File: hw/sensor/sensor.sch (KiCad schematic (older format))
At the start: 30 parts, among them J1 TC2030-CTX, U1 NRF52811-QFAA, U2 SHT3x-DIS, Y1 32.768kHz, Y2 32MHz

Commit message: Finished ostur sensor and released to oshpark
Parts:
- AE1: DKPN (none) -> 535-14095-1-ND; MPN (none) -> AMCA31-2R450G-S1F-T3
- BT1: DKPN (none) -> BK-912-ND; MPN (none) -> BK-912
- D1, D2: DKPN (none) -> 1516-1216-1-ND; MPN (none) -> QBLP595-IG
- R1, R2: DKPN (none) -> 311-10KJRCT-ND; MPN (none) -> RC0402JR-0710KL
- R5: DKPN (none) -> 1276-3480-1-ND; MPN (none) -> RC1005J000CS
- U2: DKPN (none) -> 1649-1082-1-ND; MPN (none) -> SHT30-DIS-P2.5KS
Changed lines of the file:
@@
 F 2 "alvarop:AMCA31-2R450G-S1F-T3" H 12900 5950 50  0001 C CNN
 F 3 "~" H 12900 5950 50  0001 C CNN
+F 4 "535-14095-1-ND" H 12900 5950 50  0001 C CNN "DKPN"
+F 5 "AMCA31-2R450G-S1F-T3" H 12900 5950 50  0001 C CNN "MPN"
 	1    12900 5950
 	1    0    0    -1
@@
 F 2 "Resistor_SMD:R_0402_1005Metric" H 12500 6250 50  0001 C CNN
 F 3 "~" H 12500 6250 50  0001 C CNN
+F 4 "1276-3480-1-ND" H 12500 6250 50  0001 C CNN "DKPN"
+F 5 "RC1005J000CS" H 12500 6250 50  0001 C CNN "MPN"
 	1    12500 6250
 	0    1    1    0
@@
 F 2 "alvarop:BK-912" V 4400 2410 50  0001 C CNN
 F 3 "~" V 4400 2410 50  0001 C CNN
+F 4 "BK-912-ND" H 4400 2350 50  0001 C CNN "DKPN"
+F 5 "BK-912" H 4400 2350 50  0001 C CNN "MPN"
 	1    4400 2350
 	1    0    0    -1
@@
 F 2 "Resistor_SMD:R_0402_1005Metric" H 5050 6200 50  0001 C CNN
 F 3 "~" H 5050 6200 50  0001 C CNN
+F 4 "311-10KJRCT-ND" H 5050 6200 50  0001 C CNN "DKPN"
+F 5 "RC0402JR-0710KL" H 5050 6200 50  0001 C CNN "MPN"
 	1    5050 6200
 	-1   0    0    1
@@
 F 2 "Resistor_SMD:R_0402_1005Metric" H 4800 6200 50  0001 C CNN
 F 3 "~" H 4800 6200 50  0001 C CNN
+F 4 "311-10KJRCT-ND" H 4800 6200 50  0001 C CNN "DKPN"
+F 5 "RC0402JR-0710KL" H 4800 6200 50  0001 C CNN "MPN"
 	1    4800 6200
 	-1   0    0    1
@@
 F 2 "LED_SMD:LED_0402_1005Metric" H 4800 6600 50  0001 C CNN
 F 3 "~" H 4800 6600 50  0001 C CNN
+F 4 "1516-1216-1-ND" H 4800 6600 50  0001 C CNN "DKPN"
+F 5 "QBLP595-IG" H 4800 6600 50  0001 C CNN "MPN"
 	1    4800 6600
 	0    -1   -1   0
@@
 F 2 "LED_SMD:LED_0402_1005Metric" H 5050 6600 50  0001 C CNN
 F 3 "~" H 5050 6600 50  0001 C CNN
+F 4 "1516-1216-1-ND" H 5050 6600 50  0001 C CNN "DKPN"
+F 5 "QBLP595-IG" H 5050 6600 50  0001 C CNN "MPN"
 	1    5050 6600
 	0    -1   -1   0
@@
 F 2 "alvarop:SHT3x" H 8950 9050 60  0001 C CNN
 F 3 "" H 8950 9050 60  0000 C CNN
+F 4 "1649-1082-1-ND" H 9200 9050 50  0001 C CNN "DKPN"
+F 5 "SHT30-DIS-P2.5KS" H 9200 9050 50  0001 C CNN "MPN"
 	1    9200 9050
 	1    0    0    -1

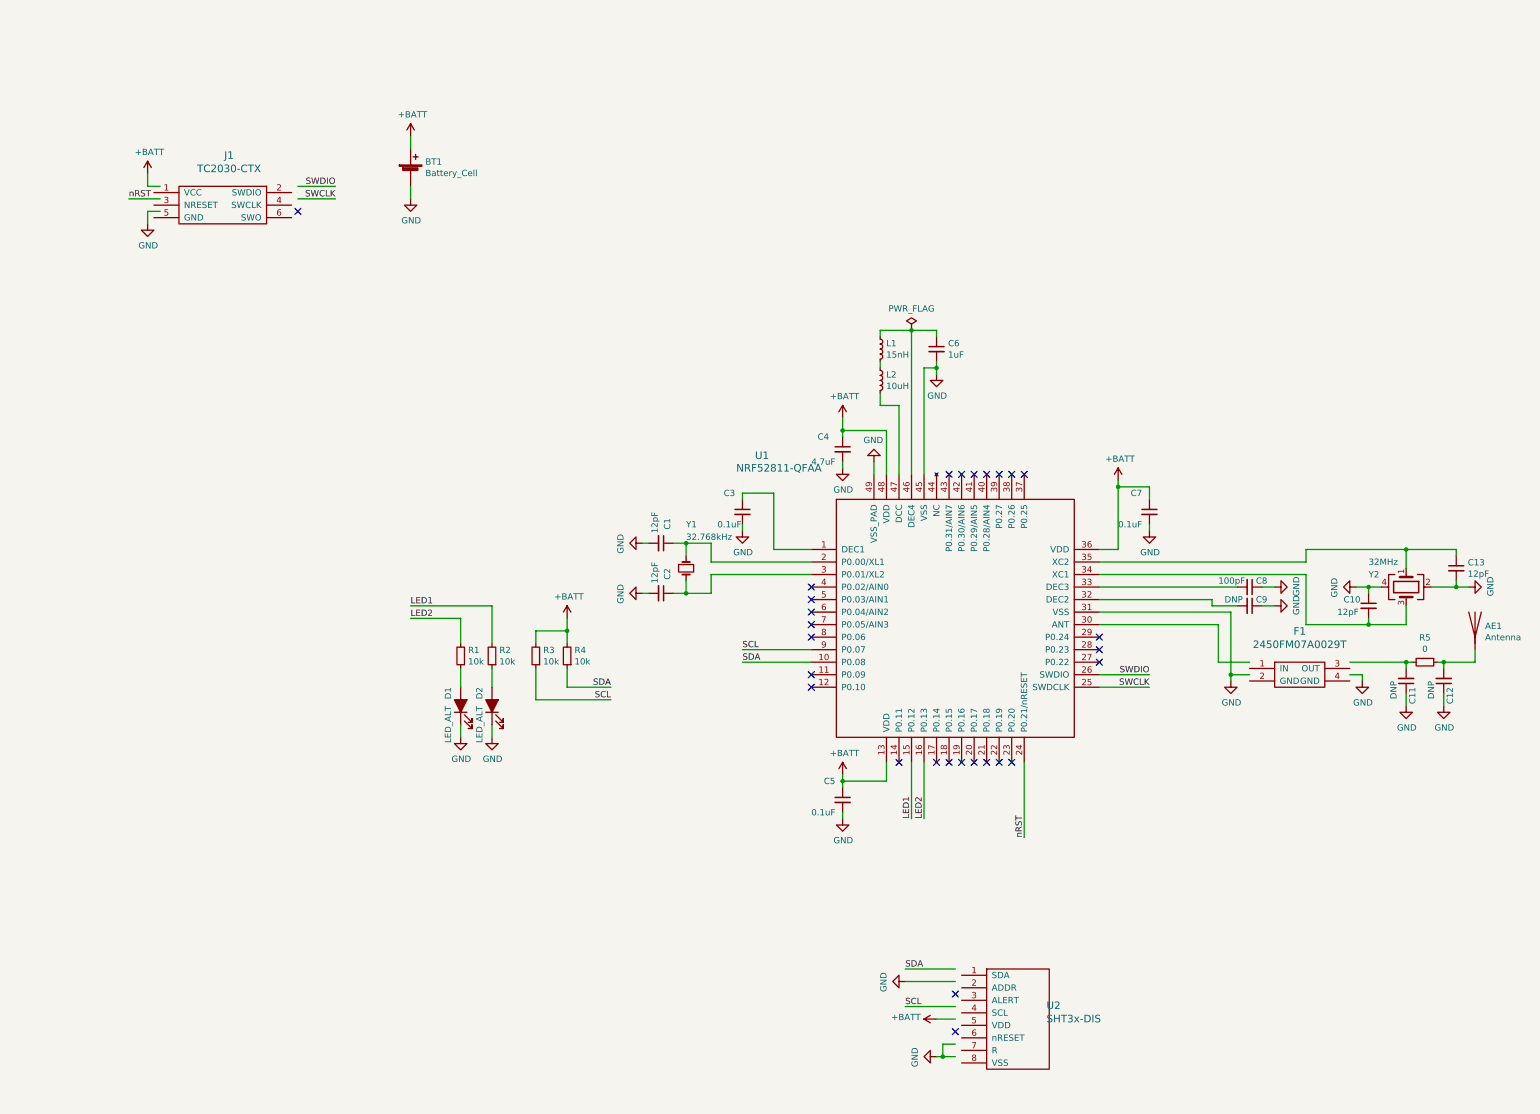
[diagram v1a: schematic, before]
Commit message: Released Ostur Sensor v1.1 to JLCPCB
Changes:
* Changed to 4 layer board for better RF performance
* Changed RF trace to match 50Ohms on JLCPCB's JLC7628 stackup
* Added decoupling capacitor for SHT3x
* Changed I2C pull-ups to 0402's
* Fixed silkscreen issues
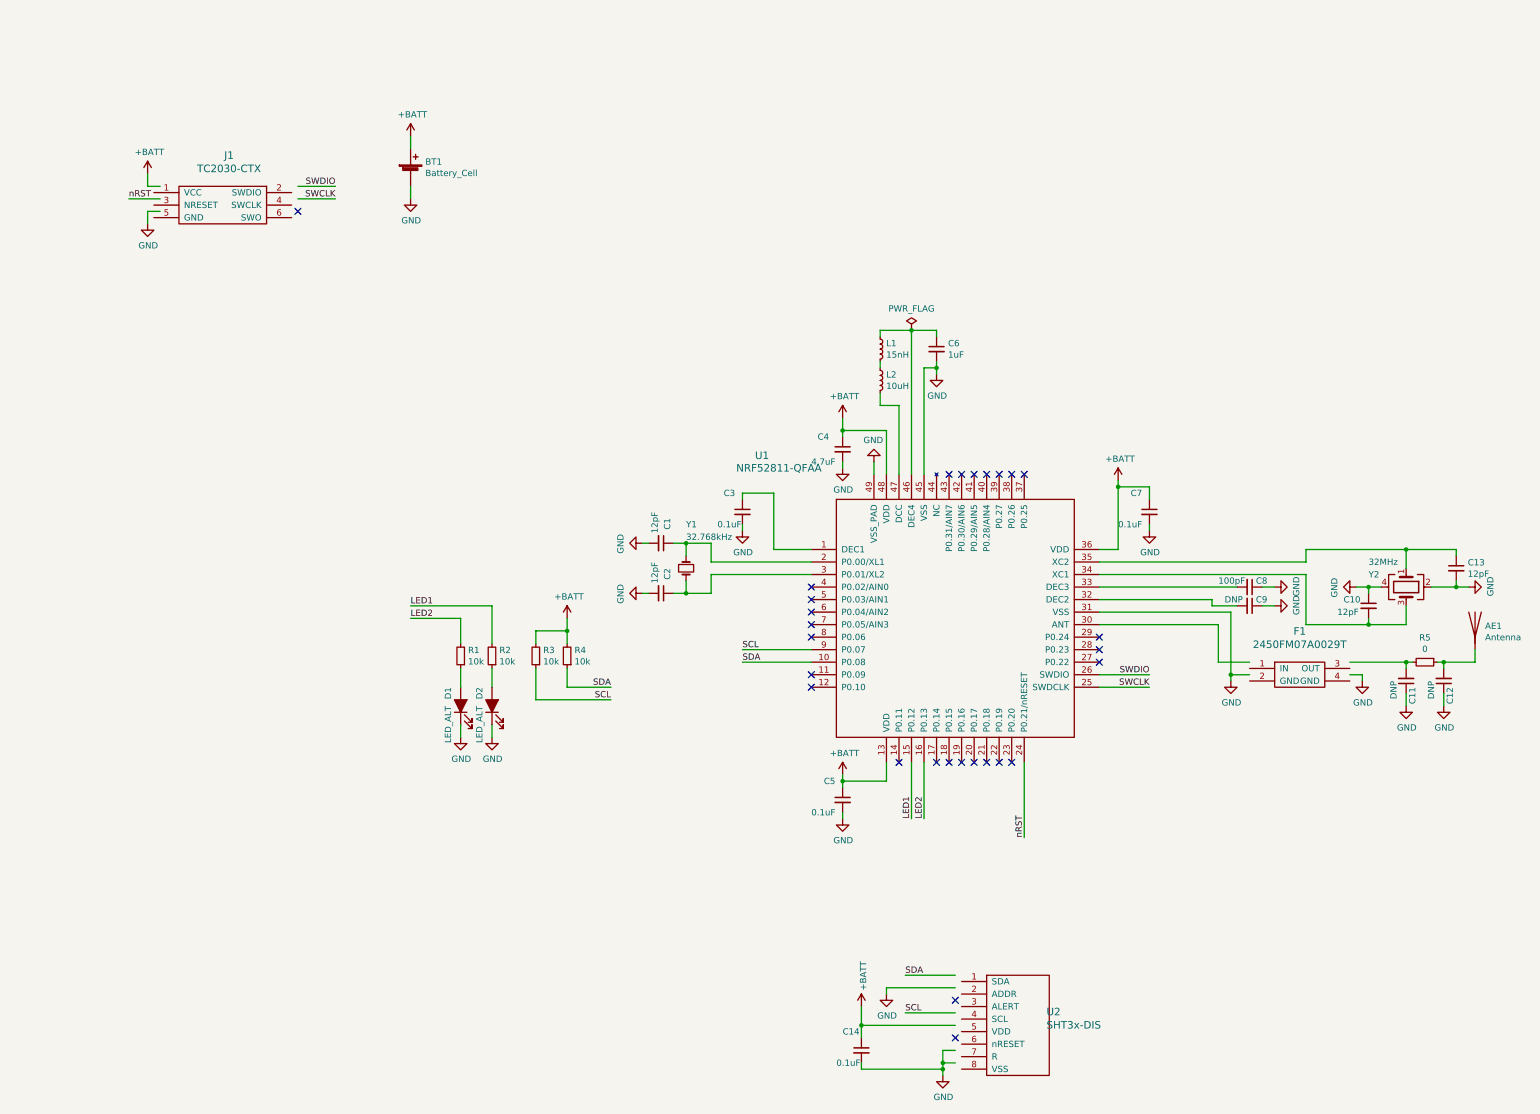
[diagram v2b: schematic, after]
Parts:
- added C14: 0.1uF, Capacitor_SMD:C_0402_1005Metric, symbol Device:C_Small
- R3, R4: footprint Resistor_SMD:R_0603_1608Metric -> Resistor_SMD:R_0402_1005Metric; DKPN (none) -> 311-10KJRCT-ND; MPN (none) -> RC0402JR-0710KL
- U1: footprint Package_DFN_QFN:QFN-48-1EP_6x6mm_P0.4mm_EP4.6x4.6mm -> alvarop:NRF52811-QFN48
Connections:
- wire segments 129 -> 135
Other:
- moved on the sheet: U2
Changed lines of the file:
@@
 EESchema Schematic File Version 4
 LIBS:sensor-cache
-EELAYER 29 0
+EELAYER 30 0
 EELAYER END
 $Descr A3 16535 11693
@@
 Sheet 1 1
 Title "Ostur Sensor"
-Date "2019-06-29"
-Rev "1.0"
+Date "2019-10-10"
+Rev "1.1"
 Comp "@alvaroprieto"
 Comment1 ""
@@
 	2400 2450 2300 2450
 Wire Wire Line
-	2300 2450 2300 2350
-Wire Wire Line
 	2400 2550 2150 2550
 Wire Wire Line
 	2400 2650 2300 2650
-Wire Wire Line
-	2300 2650 2300 2750
 $Comp
 L power:GND #PWR02
@@
 F 0 "U1" H 7150 7200 60  0000 L CNN
 F 1 "NRF52811-QFAA" H 7000 7100 60  0000 L CNN
-F 2 "Package_DFN_QFN:QFN-48-1EP_6x6mm_P0.4mm_EP4.6x4.6mm" H 7600 6450 50  0001 C CNN
+F 2 "alvarop:NRF52811-QFN48" H 7600 6450 50  0001 C CNN
 F 3 "" H 7600 6450 50  0001 C CNN
 F 4 "‎1490-1075-1-ND‎" H 8750 5900 50  0001 C CNN "DKPN"
@@
 L power:+BATT #PWR018
 U 1 1 5D1FA7C1
-P 8600 9100
-F 0 "#PWR018" H 8600 8950 50  0001 C CNN
-F 1 "+BATT" V 8615 9227 50  0000 L CNN
-F 2 "" H 8600 9100 50  0001 C CNN
-F 3 "" H 8600 9100 50  0001 C CNN
-	1    8600 9100
-	0    -1   -1   0
+P 8000 9000
+F 0 "#PWR018" H 8000 8850 50  0001 C CNN
+F 1 "+BATT" V 8015 9127 50  0000 L CNN
+F 2 "" H 8000 9000 50  0001 C CNN
+F 3 "" H 8000 9000 50  0001 C CNN
+	1    8000 9000
+	1    0    0    -1
 $EndComp
 $Comp
 L power:GND #PWR019
 U 1 1 5D1FD0BD
-P 8600 9400
-F 0 "#PWR019" H 8600 9150 50  0001 C CNN
-F 1 "GND" H 8605 9227 50  0000 C CNN
-F 2 "" H 8600 9400 50  0001 C CNN
-F 3 "" H 8600 9400 50  0001 C CNN
-	1    8600 9400
-	0    1    1    0
-$EndComp
-Wire Wire Line
-	8750 9400 8650 9400
-Wire Wire Line
-	8750 9100 8600 9100
-Wire Wire Line
-	8750 8700 8350 8700
-Wire Wire Line
-	8750 8800 8350 8800
-Wire Wire Line
-	8750 9000 8350 9000
-Wire Wire Line
-	8650 9300 8650 9400
-Wire Wire Line
-	8650 9300 8750 9300
-Connection ~ 8650 9400
-Wire Wire Line
-	8650 9400 8600 9400
+P 8650 9550
+F 0 "#PWR019" H 8650 9300 50  0001 C CNN
+F 1 "GND" H 8655 9377 50  0000 C CNN
+F 2 "" H 8650 9550 50  0001 C CNN
+F 3 "" H 8650 9550 50  0001 C CNN
+	1    8650 9550
+	1    0    0    -1
+$EndComp
+Wire Wire Line
+	8750 9450 8650 9450
+Wire Wire Line
+	8750 8750 8350 8750
+Wire Wire Line
+	8750 9050 8350 9050
+Wire Wire Line
+	8650 9350 8650 9450
+Wire Wire Line
+	8650 9350 8750 9350
+Connection ~ 8650 9450
+Wire Wire Line
+	8650 9450 8650 9500
 $Comp
 L power:GND #PWR016
 U 1 1 5D22F6D9
-P 8350 8800
-F 0 "#PWR016" H 8350 8550 50  0001 C CNN
-F 1 "GND" H 8355 8627 50  0000 C CNN
-F 2 "" H 8350 8800 50  0001 C CNN
-F 3 "" H 8350 8800 50  0001 C CNN
-	1    8350 8800
-	0    1    1    0
-$EndComp
-NoConn ~ 8750 8900
-Text Label 8350 8700 0    50   ~ 0
+P 8200 8900
+F 0 "#PWR016" H 8200 8650 50  0001 C CNN
+F 1 "GND" H 8205 8727 50  0000 C CNN
+F 2 "" H 8200 8900 50  0001 C CNN
+F 3 "" H 8200 8900 50  0001 C CNN
+	1    8200 8900
+	1    0    0    -1
+$EndComp
+NoConn ~ 8750 8950
+Text Label 8350 8750 0    50   ~ 0
 SDA
-Text Label 8350 9000 0    50   ~ 0
+Text Label 8350 9050 0    50   ~ 0
 SCL
 NoConn ~ 9900 6250
@@
 F 0 "R4" H 5591 6154 50  0000 R CNN
 F 1 "10k" H 5591 6245 50  0000 R CNN
-F 2 "Resistor_SMD:R_0603_1608Metric" H 5650 6200 50  0001 C CNN
+F 2 "Resistor_SMD:R_0402_1005Metric" H 5650 6200 50  0001 C CNN
 F 3 "~" H 5650 6200 50  0001 C CNN
+F 4 "311-10KJRCT-ND" H 5650 6200 50  0001 C CNN "DKPN"
+F 5 "RC0402JR-0710KL" H 5650 6200 50  0001 C CNN "MPN"
 	1    5650 6200
 	-1   0    0    1
@@
 F 0 "R3" H 5341 6154 50  0000 R CNN
 F 1 "10k" H 5341 6245 50  0000 R CNN
-F 2 "Resistor_SMD:R_0603_1608Metric" H 5400 6200 50  0001 C CNN
+F 2 "Resistor_SMD:R_0402_1005Metric" H 5400 6200 50  0001 C CNN
 F 3 "~" H 5400 6200 50  0001 C CNN
+F 4 "311-10KJRCT-ND" H 5400 6200 50  0001 C CNN "DKPN"
+F 5 "RC0402JR-0710KL" H 5400 6200 50  0001 C CNN "MPN"
 	1    5400 6200
 	-1   0    0    1
@@
 L alvarop:SHT3x-DIS U2
 U 1 1 5D1DABB6
-P 9200 9050
-F 0 "U2" H 9478 9108 60  0000 L CNN
-F 1 "SHT3x-DIS" H 9478 9002 60  0000 L CNN
-F 2 "alvarop:SHT3x" H 8950 9050 60  0001 C CNN
-F 3 "" H 8950 9050 60  0000 C CNN
-F 4 "1649-1082-1-ND" H 9200 9050 50  0001 C CNN "DKPN"
-F 5 "SHT30-DIS-P2.5KS" H 9200 9050 50  0001 C CNN "MPN"
-	1    9200 9050
-	1    0    0    -1
-$EndComp
-NoConn ~ 8750 9200
+P 9200 9100
+F 0 "U2" H 9478 9158 60  0000 L CNN
+F 1 "SHT3x-DIS" H 9478 9052 60  0000 L CNN
+F 2 "alvarop:SHT3x" H 8950 9100 60  0001 C CNN
+F 3 "" H 8950 9100 60  0000 C CNN
+F 4 "1649-1082-1-ND" H 9200 9100 50  0001 C CNN "DKPN"
+F 5 "SHT30-DIS-P2.5KS" H 9200 9100 50  0001 C CNN "MPN"
+	1    9200 9100
+	1    0    0    -1
+$EndComp
+NoConn ~ 8750 9250
 Text Label 7050 6250 0    50   ~ 0
 SDA
 NoConn ~ 7600 6050
+$Comp
+L Device:C_Small C14
+U 1 1 5D9A55D5
+P 8000 9350
+F 0 "C14" H 7850 9500 50  0000 L CNN
+F 1 "0.1uF" H 7800 9250 50  0000 L CNN
+F 2 "Capacitor_SMD:C_0402_1005Metric" H 8000 9350 50  0001 C CNN
+F 3 "~" H 8000 9350 50  0001 C CNN
+F 4 "490-1318-1-ND" H 8000 9350 50  0001 C CNN "DKPN"
+F 5 "GRM155R61A104KA01D" H 8000 9350 50  0001 C CNN "MPN"
+	1    8000 9350
+	1    0    0    -1
+$EndComp
+Wire Wire Line
+	8000 9250 8000 9150
+Wire Wire Line
+	2300 2350 2300 2450
+Wire Wire Line
+	2300 2650 2300 2750
+Wire Wire Line
+	8000 9150 8000 9000
+Wire Wire Line
+	8000 9150 8750 9150
+Wire Wire Line
+	8200 8900 8200 8850
+Wire Wire Line
+	8200 8850 8750 8850
+Connection ~ 8000 9150
+Wire Wire Line
+	8000 9450 8000 9500
+Wire Wire Line
+	8000 9500 8650 9500
+Connection ~ 8650 9500
+Wire Wire Line
+	8650 9500 8650 9550
 $EndSCHEMATC

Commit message: Not sure why I never committed this.
Using NRF52805
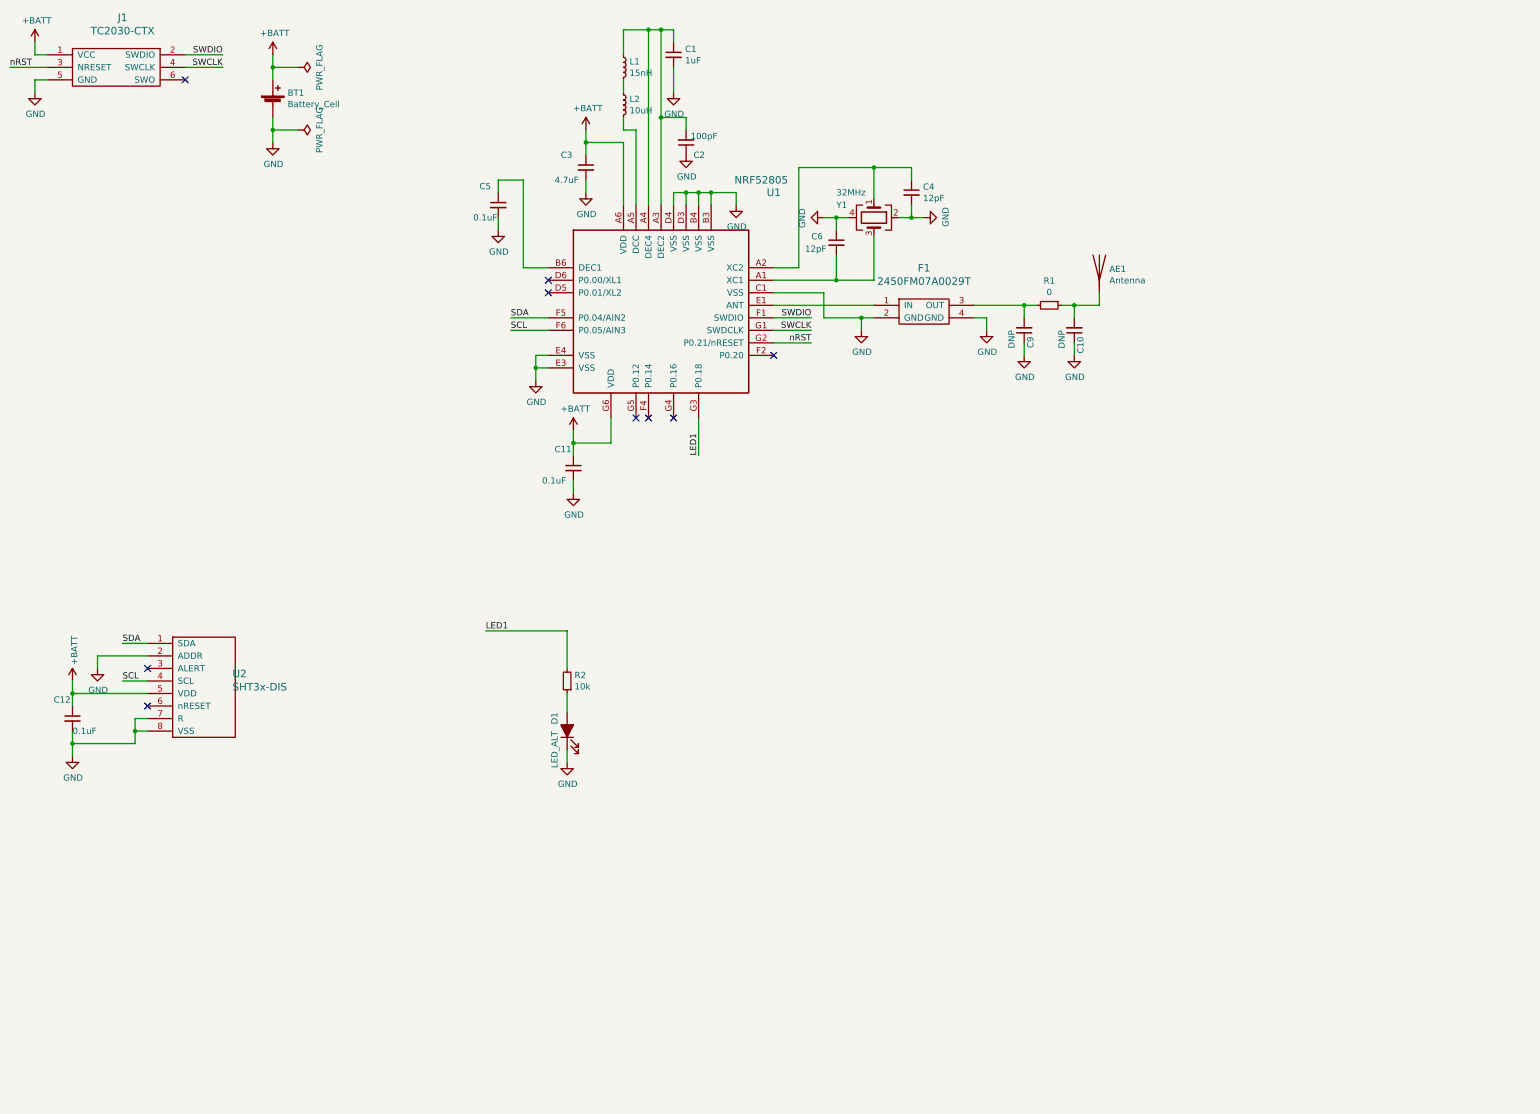
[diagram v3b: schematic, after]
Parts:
- removed C1, C2: 12pF, Capacitor_SMD:C_0402_1005Metric, symbol Device:C_Small
- removed C7: 0.1uF, Capacitor_SMD:C_0402_1005Metric, symbol Device:C_Small
- removed C9: DNP, Capacitor_SMD:C_0402_1005Metric, symbol Device:C_Small
- removed D1: LED_ALT, LED_SMD:LED_0402_1005Metric, symbol Device:LED_ALT
- removed R1, R3, R4: 10k, Resistor_SMD:R_0402_1005Metric, symbol Device:R_Small
- removed U1: NRF52811-QFAA, alvarop:NRF52811-QFN48, symbol alvarop:NRF52811-QFAA
- removed Y1: 32.768kHz, Crystal:Crystal_SMD_3215-2Pin_3.2x1.5mm, symbol Device:Crystal_Small
- added U1: NRF52805, alvarop:NRF52805, symbol alvarop:NRF52805
- BT1: footprint alvarop:BK-912 -> alvarop:BAT-HLD-001-THM; DKPN BK-912-ND -> BAT-HLD-001-THM-ND; MPN BK-912 -> BATT-HLD-001-THM
- renumbered C6 to C1, C12 to C10, C5 to C11, C14 to C12, C8 to C2, C4 to C3, C13 to C4, C3 to C5, C10 to C6, C11 to C9, D2 to D1, R5 to R1, Y2 to Y1
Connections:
- net labels removed: LED2
- wire segments 135 -> 113
- no-connect marks 28 -> 9
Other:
- moved on the sheet: AE1, BT1, C1, C10, C11, C12, C2, C3, C4, C5, C6, C9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
